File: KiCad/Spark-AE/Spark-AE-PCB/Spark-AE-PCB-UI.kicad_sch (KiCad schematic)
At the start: 56 parts, among them Q2 2N3904, Q3 2N3904, SW1 SW_Push, SW2 SW_Push, U2 MCP6002T-I_MS, U3 Driver_LED_PCA9633PW,118

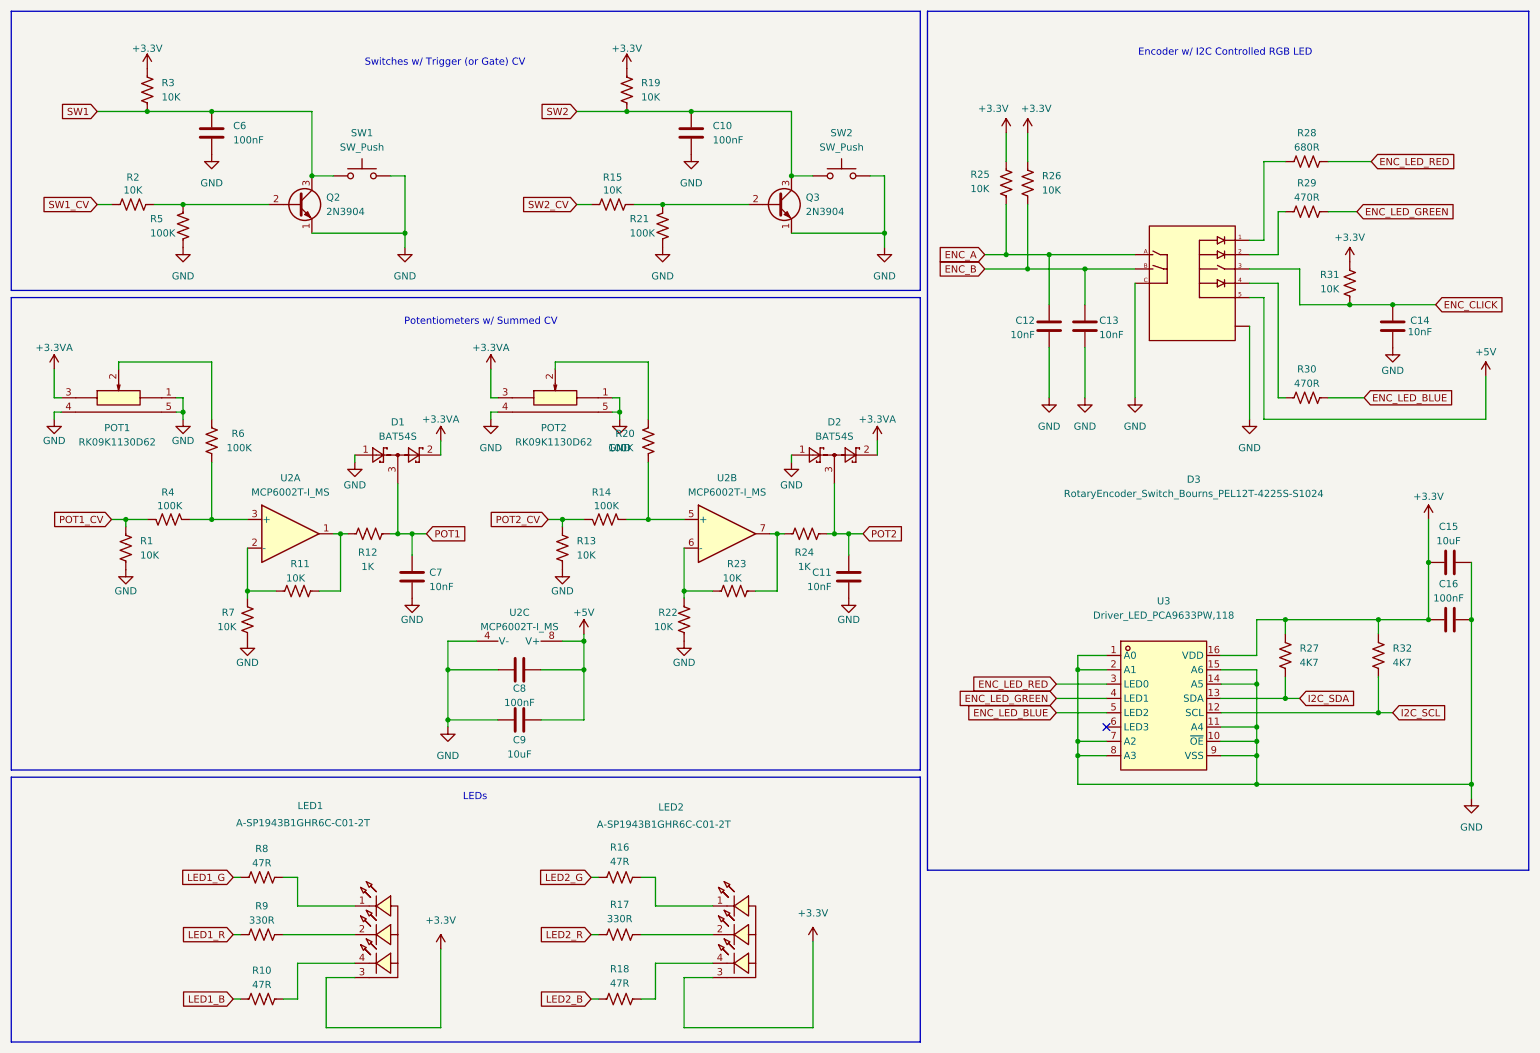
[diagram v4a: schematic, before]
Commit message: pcb layout complete. ready for final pre-fab confirmation.
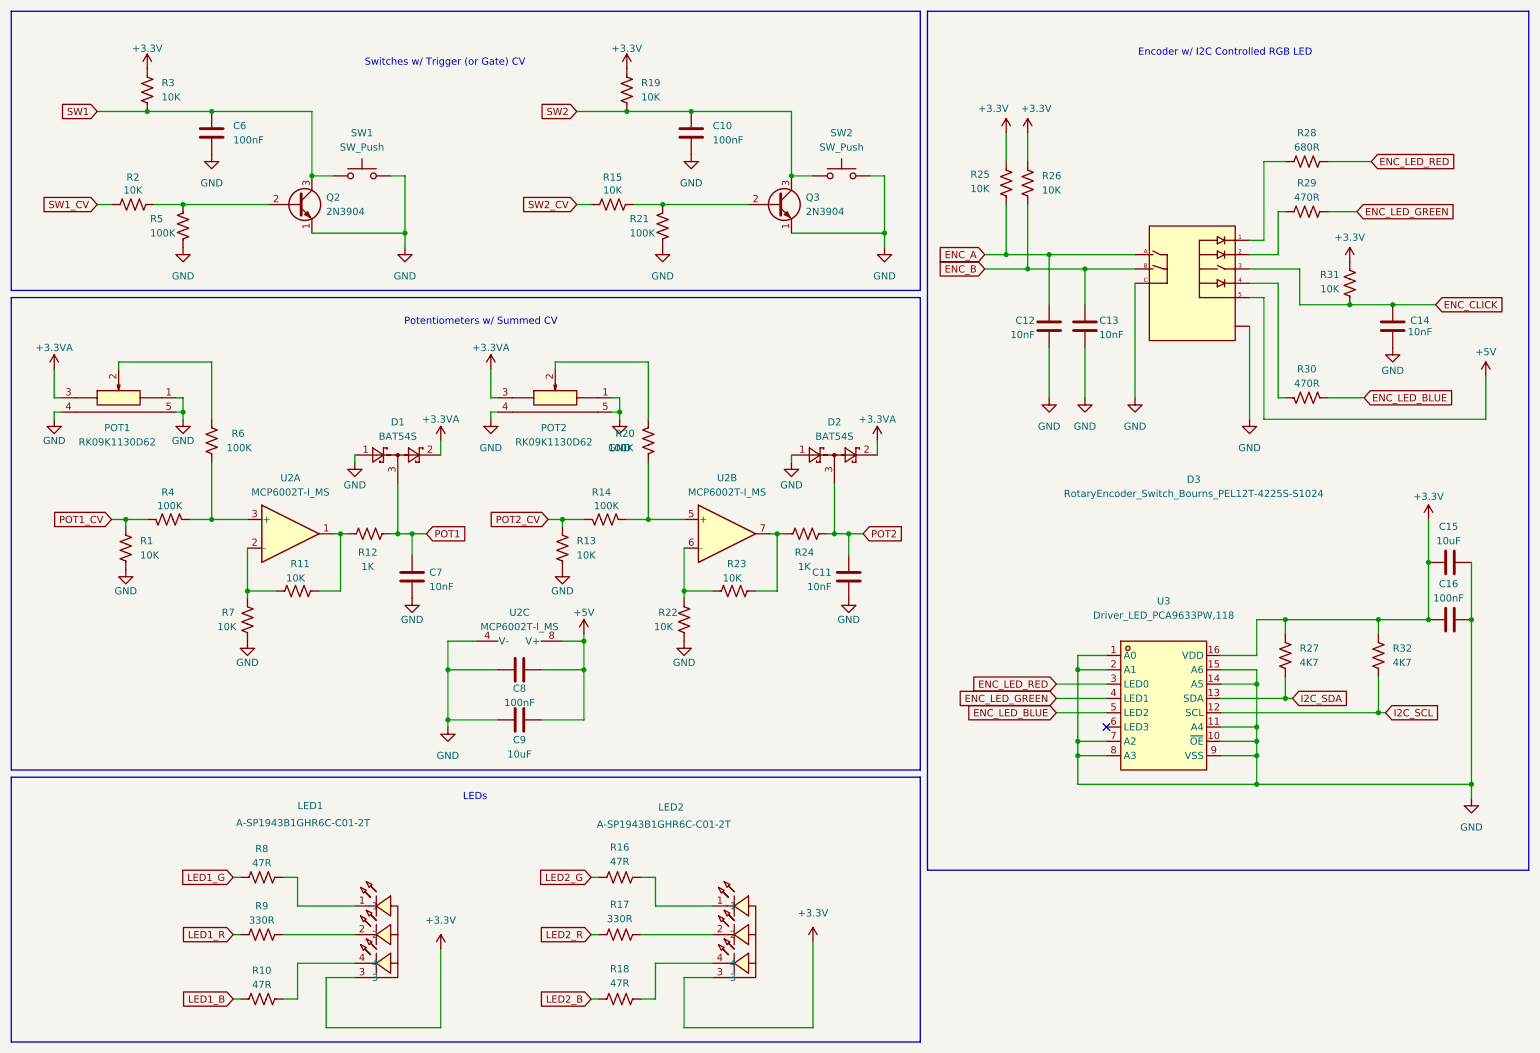
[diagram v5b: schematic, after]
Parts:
- LED1, LED2: symbol clectric-diy:LED-SMD_4P-L1.6-W1.5-BL_A-SP1943B1GHR6C-C01-2T -> clectric-diy:LED_ARGB_Amicc_A-SP1943B1GHR6C-C01-2T
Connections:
- net ENC_LED_BLUE: now also R30.1; no longer R30.2
- net at D3.4: now also R30.2; no longer R30.1
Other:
- moved on the sheet: R30
